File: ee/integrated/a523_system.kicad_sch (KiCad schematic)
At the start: 16 parts, among them U201 A523, Y201 24MHz / CL20pF / 20ppm, Y202 32.768kHz / CL12.5pF / 20ppm

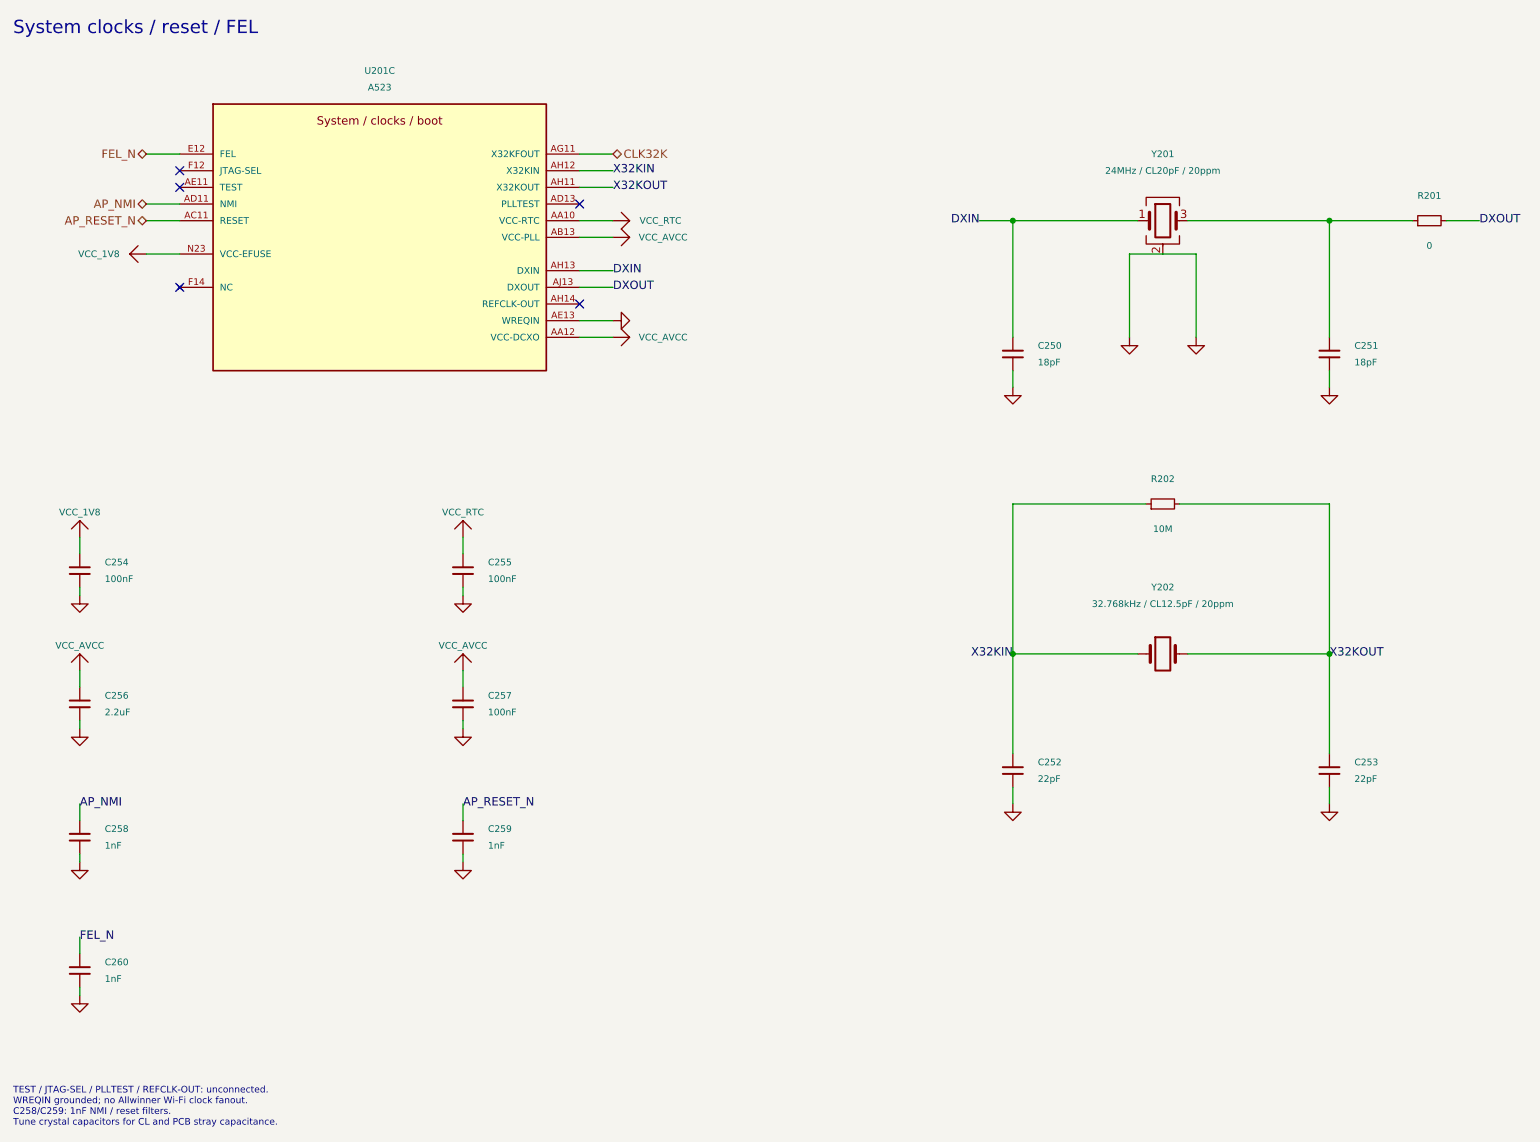
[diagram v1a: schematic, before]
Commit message: Removed USB sheets and moved the parts to the main sheets.
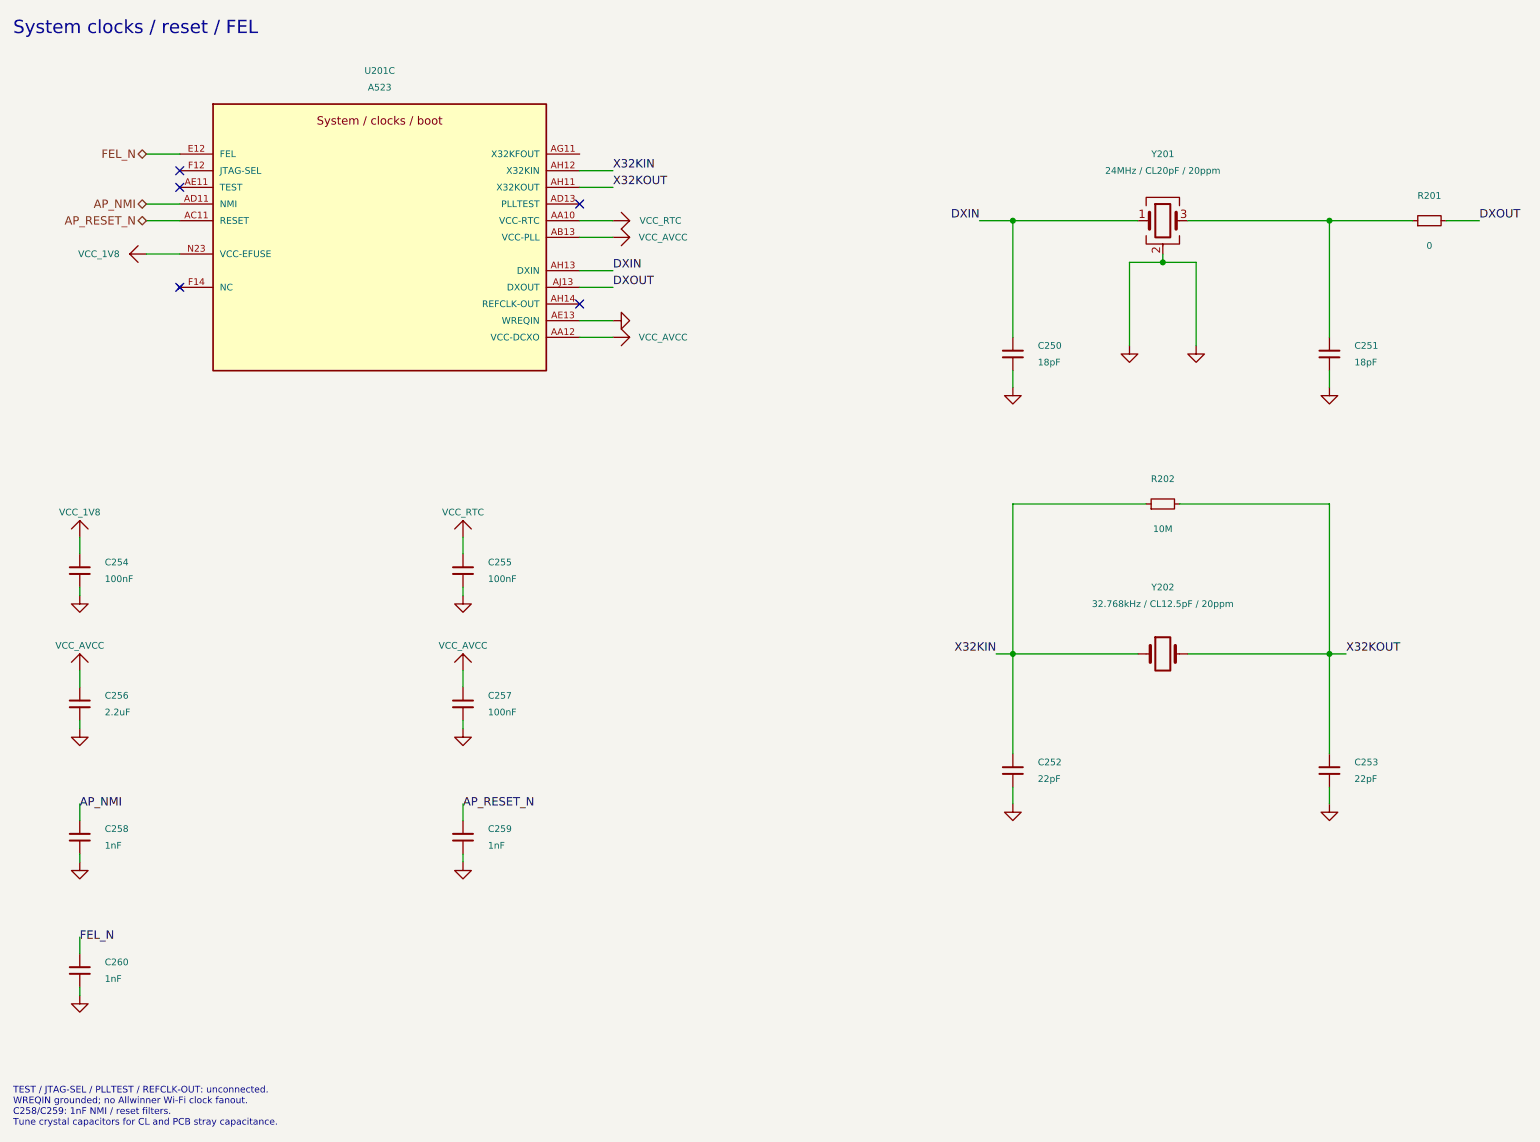
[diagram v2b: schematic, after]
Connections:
- net CLK32K: no longer names the net of U201.AG11 (X32KFOUT)
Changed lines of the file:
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@@
 	)
 	(junction
+		(at 195.58 52.07)
+		(diameter 0)
+		(color 0 0 0 0)
+	)
+	(junction
 		(at 172.72 111.76)
 		(diameter 0)
@@
 	(wire
 		(pts
-			(xy 200.66 50.8) (xy 200.66 63.5)
+			(xy 200.66 52.07) (xy 200.66 64.77)
 		)
 		(stroke
@@
 	(wire
 		(pts
-			(xy 106.68 35.56) (xy 111.76 35.56)
+			(xy 193.04 88.9) (xy 172.72 88.9)
 		)
 		(stroke
@@
 	(wire
 		(pts
-			(xy 193.04 88.9) (xy 172.72 88.9)
+			(xy 195.58 52.07) (xy 195.58 50.8)
 		)
 		(stroke
@@
 	(wire
 		(pts
+			(xy 170.18 111.76) (xy 172.72 111.76)
+		)
+		(stroke
+			(width 0)
+			(type default)
+		)
+	)
+	(wire
+		(pts
 			(xy 220.98 45.72) (xy 233.68 45.72)
 		)
@@
 	(wire
 		(pts
-			(xy 195.58 50.8) (xy 190.5 50.8)
+			(xy 195.58 52.07) (xy 190.5 52.07)
 		)
 		(stroke
@@
 	(wire
 		(pts
-			(xy 190.5 50.8) (xy 190.5 63.5)
+			(xy 190.5 52.07) (xy 190.5 64.77)
 		)
 		(stroke
@@
 	(wire
 		(pts
+			(xy 223.52 111.76) (xy 220.98 111.76)
+		)
+		(stroke
+			(width 0)
+			(type default)
+		)
+	)
+	(wire
+		(pts
 			(xy 172.72 132.08) (xy 172.72 134.62)
 		)
@@
 	(wire
 		(pts
-			(xy 195.58 50.8) (xy 200.66 50.8)
+			(xy 195.58 52.07) (xy 200.66 52.07)
 		)
 		(stroke
@@
 				(size 1.27 1.27)
 			)
-			(justify right)
+			(justify right bottom)
 		)
 	)
@@
 				(size 1.27 1.27)
 			)
-			(justify left)
+			(justify left bottom)
 		)
 	)
 	(label "X32KIN"
-		(at 172.72 111.76 180)
+		(at 170.18 111.76 180)
 		(effects
 			(font
 				(size 1.27 1.27)
 			)
-			(justify right)
+			(justify right bottom)
 		)
 	)
@@
 				(size 1.27 1.27)
 			)
-			(justify left)
+			(justify left bottom)
 		)
 	)
@@
 				(size 1.27 1.27)
 			)
-			(justify left)
+			(justify left bottom)
 		)
 	)
 	(label "X32KOUT"
-		(at 220.98 111.76 0)
+		(at 223.52 111.76 0)
 		(effects
 			(font
 				(size 1.27 1.27)
 			)
-			(justify left)
+			(justify left bottom)
 		)
 	)
@@
 				(size 1.27 1.27)
 			)
-			(justify left)
+			(justify left bottom)
 		)
 	)
@@
 				(size 1.27 1.27)
 			)
-			(justify left)
+			(justify left bottom)
 		)
 	)
@@
 		)
 	)
-	(hierarchical_label "CLK32K"
-		(shape bidirectional)
-		(at 111.76 35.56 0)
-		(effects
-			(font
-				(size 1.27 1.27)
-			)
-			(justify left)
-		)
-	)
 	(hierarchical_label "FEL_N"
 		(shape bidirectional)
@@
 	(symbol
 		(lib_id "power:GND")
-		(at 200.66 63.5 0)
+		(at 200.66 64.77 0)
 		(unit 1)
 		(body_style 1)
@@
 		(dnp no)
 		(property "Reference" "#PWR0297774486"
-			(at 200.66 63.5 0)
+			(at 200.66 64.77 0)
 			(hide yes)
 			(show_name no)
@@
 		)
 		(property "Value" "GND"
-			(at 200.66 67.31 0)
+			(at 200.66 68.58 0)
 			(hide yes)
 			(show_name no)
@@
 		)
 		(property "Footprint" ""
-			(at 200.66 63.5 0)
+			(at 200.66 64.77 0)
 			(show_name no)
 			(do_not_autoplace no)
@@
 		)
 		(property "Datasheet" ""
-			(at 200.66 63.5 0)
+			(at 200.66 64.77 0)
 			(show_name no)
 			(do_not_autoplace no)
@@
 		)
 		(property "Description" ""
-			(at 200.66 63.5 0)
+			(at 200.66 64.77 0)
 			(show_name no)
 			(do_not_autoplace no)
@@
 	(symbol
 		(lib_id "power:GND")
-		(at 190.5 63.5 0)
+		(at 190.5 64.77 0)
 		(unit 1)
 		(body_style 1)
@@
 		(dnp no)
 		(property "Reference" "#PWR0837745405"
-			(at 190.5 63.5 0)
+			(at 190.5 64.77 0)
 			(hide yes)
 			(show_name no)
@@
 		)
 		(property "Value" "GND"
-			(at 190.5 67.31 0)
+			(at 190.5 68.58 0)
 			(hide yes)
 			(show_name no)
@@
 		)
 		(property "Footprint" ""
-			(at 190.5 63.5 0)
+			(at 190.5 64.77 0)
 			(show_name no)
 			(do_not_autoplace no)
@@
 		)
 		(property "Datasheet" ""
-			(at 190.5 63.5 0)
+			(at 190.5 64.77 0)
 			(show_name no)
 			(do_not_autoplace no)
@@
 		)
 		(property "Description" ""
-			(at 190.5 63.5 0)
+			(at 190.5 64.77 0)
 			(show_name no)
 			(do_not_autoplace no)

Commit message: Worked on the layout.
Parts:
- removed C252, C253: 22pF, Capacitor_SMD:C_0402_1005Metric, symbol Device:C_Small
- removed R202: 10M, Resistor_SMD:R_0402_1005Metric, symbol Device:R_Small
- removed Y202: 32.768kHz / CL12.5pF / 20ppm, Crystal:Crystal_SMD_3215-2Pin_3.2x1.5mm, symbol Device:Crystal
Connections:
- net X32KIN: no longer names the net of U201.AH12 (X32KIN)
- net X32KOUT: no longer names the net of U201.AH11 (X32KOUT)
- no-connect marks 5 -> 7
